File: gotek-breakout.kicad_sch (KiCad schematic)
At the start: 4 parts, among them J1 FFC 10x1 0.5mm, J2 USB_A, J3 OLED, J4 Encoder

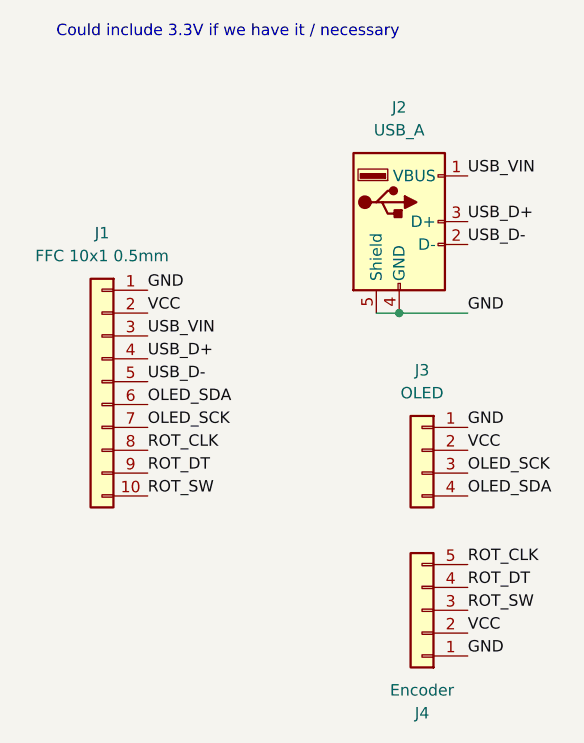
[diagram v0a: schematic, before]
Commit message: Make room for mounting
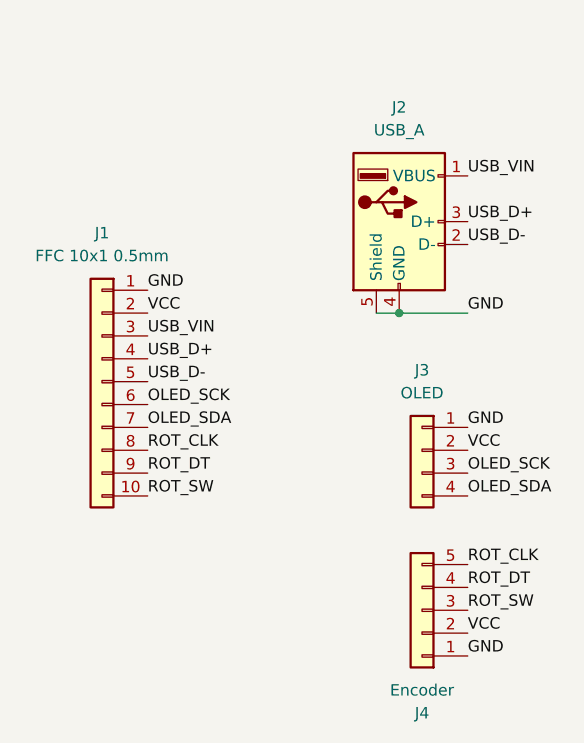
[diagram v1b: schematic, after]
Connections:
- net OLED_SCK: now also J1.6 (Pin_6); no longer J1.7 (Pin_7)
- net OLED_SDA: now also J1.7 (Pin_7); no longer J1.6 (Pin_6)
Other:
- note removed: "Could include 3.3V if we have it / necessary"
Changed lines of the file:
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@@
     (stroke (width 0) (type default))
-  )
-  (text "Could include 3.3V if we have it / necessary" (at 27.94 27.94 0)
-    (effects (font (size 1.27 1.27)) (justify left bottom))
   )
   (label "USB_VIN" (at 73.66 43.18 0) (fields_autoplaced)
@@
     (effects (font (size 1.27 1.27)) (justify left bottom))
   )
-  (label "OLED_SCK" (at 38.1 71.12 0) (fields_autoplaced)
+  (label "OLED_SCK" (at 38.1 68.58 0) (fields_autoplaced)
     (effects (font (size 1.27 1.27)) (justify left bottom))
   )
@@
     (effects (font (size 1.27 1.27)) (justify left bottom))
   )
-  (label "OLED_SDA" (at 38.1 68.58 0) (fields_autoplaced)
+  (label "OLED_SDA" (at 38.1 71.12 0) (fields_autoplaced)
     (effects (font (size 1.27 1.27)) (justify left bottom))
   )
